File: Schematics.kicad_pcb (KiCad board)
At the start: 2 copper layers, 56 parts, among them Q1 AO3400A, Q2 SI2301CDS-T1-E3, Q3 SI2301CDS-T1-E3, Q4 8050

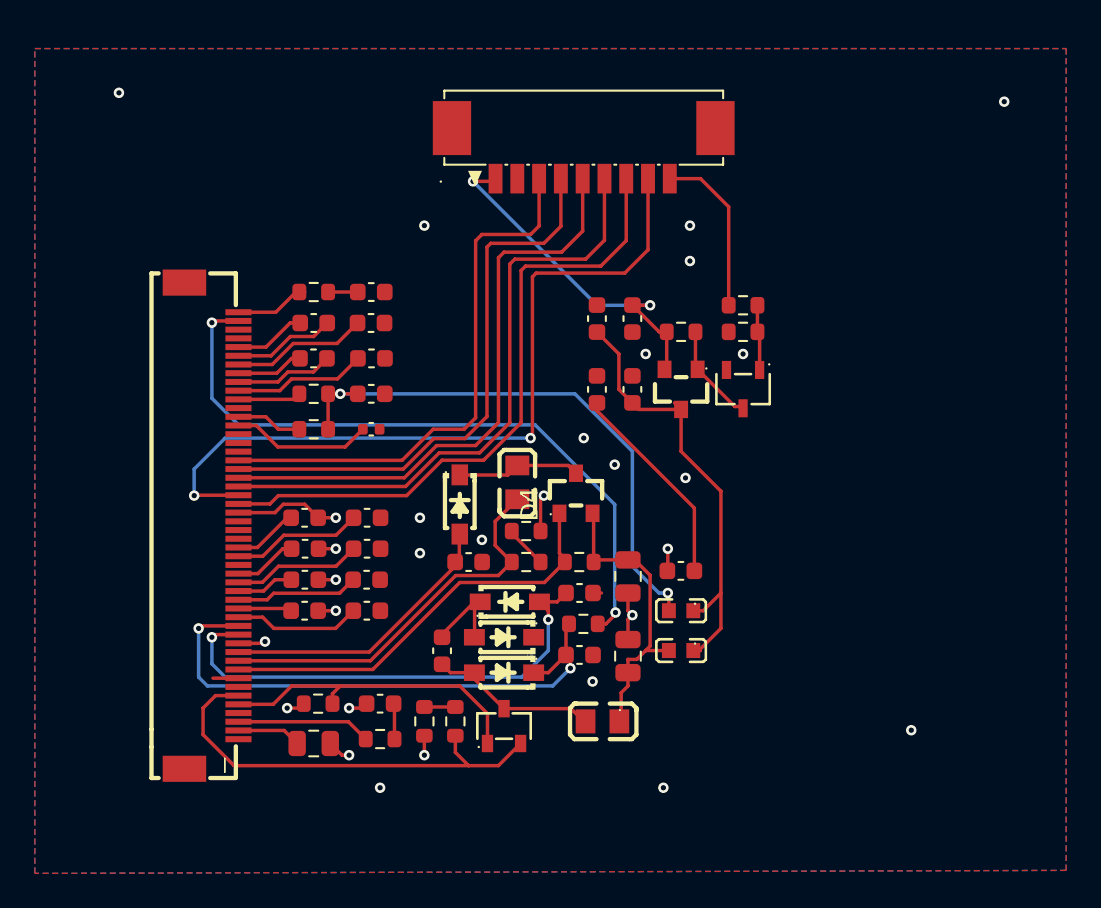
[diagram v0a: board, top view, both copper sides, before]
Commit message: added edge cuts and connected 2 unconnected ground pins
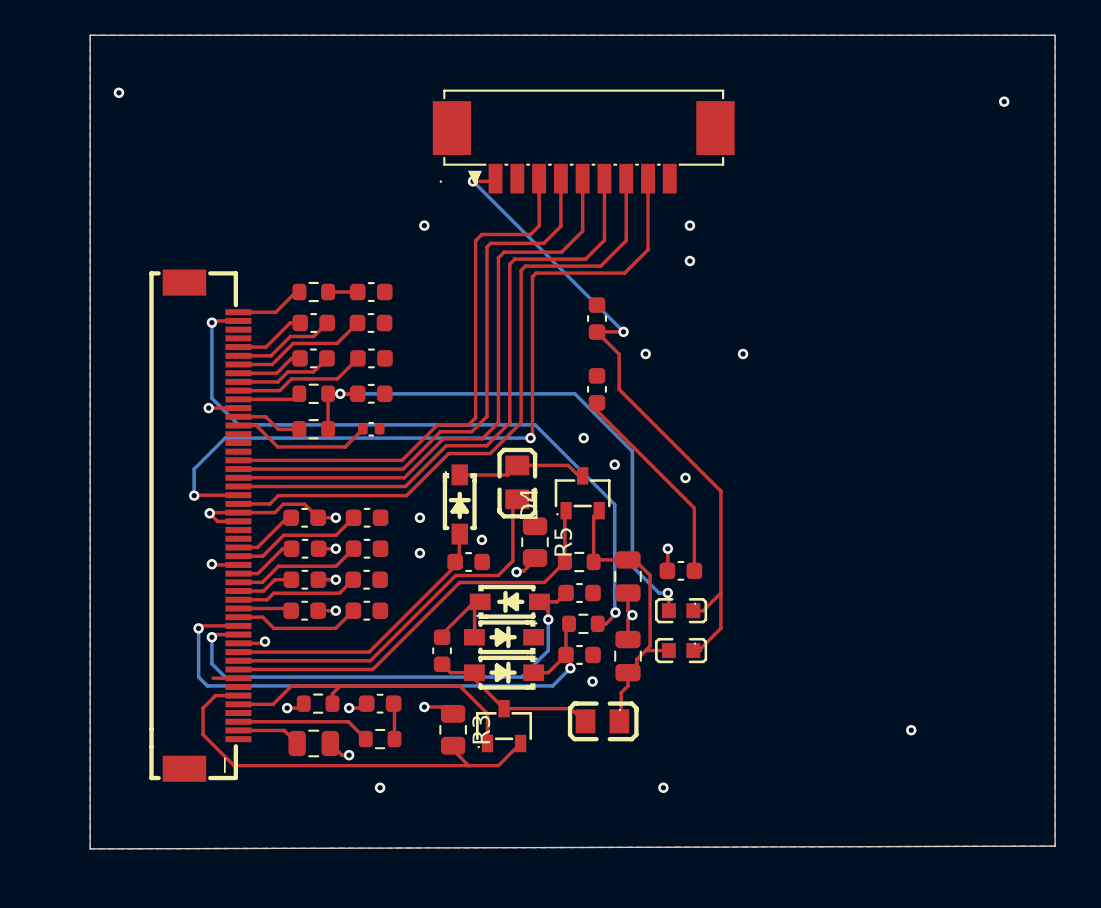
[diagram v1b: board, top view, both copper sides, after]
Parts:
- removed C22, C26: 100nF/50V, Capacitor_SMD:C_0603_1608Metric
- removed Q3: SI2301CDS-T1-E3, local:SOT-23_L2.9-W1.3-P1.90-LS2.4-BR
- removed Q4: 8050, local:SOT-23-3_L3.0-W1.7-P0.95-LS2.9-BR
- removed R11: 100K, Resistor_SMD:R_0603_1608Metric
- removed R6: 47K, Resistor_SMD:R_0603_1608Metric
- removed R7, R9: 0.1Ω, Resistor_SMD:R_0603_1608Metric
- removed R8: 10K, Resistor_SMD:R_0603_1608Metric
- Q2: value SI2301CDS-T1-E3 -> AO3401A; footprint local:SOT-23_L2.9-W1.3-P1.90-LS2.4-BR -> local:SOT-23-3_L2.9-W1.3-P1.90-LS2.4-BR
- R3, R5: value 0.1Ω -> 0.22Ω; footprint Resistor_SMD:R_0603_1608Metric -> Resistor_SMD:R_0805_2012Metric
- moved R5 0.81 mm to (77.5, 61.8), turned to -90 degrees
- moved R3 0.50 mm to (72.8, 72.6)
- moved Q2 0.38 mm to (80.2, 59.0)
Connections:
- P2 pad 1: /VCC_INT -> VCC
- R3 pad 1: Net-(R3-Pad1) -> GND
- R5 pad 1: Net-(R5-Pad1) -> /RESEC
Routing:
- net /VCC_INT: track 20.3 -> 0.00 mm, vias 2 -> 0
- net VCC: track 26.2 -> 39.3 mm, vias 0 -> 2
- net /PWR: track 10.1 -> 0.00 mm
- net GND: track 23.1 -> 29.4 mm, vias 29 -> 32
- net Net-(Q3-G): track 5.52 -> 0.00 mm
- net Net-(Q4-B): track 3.86 -> 0.00 mm
- net /RESEC: track 22.6 -> 25.2 mm
- net Net-(R5-Pad1): track 2.46 -> 0.00 mm
- net Net-(R3-Pad1): track 1.78 -> 0.00 mm
- net /RESEH: track 25.4 -> 24.8 mm
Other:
- board outline added: 55.4 x 46.7 mm

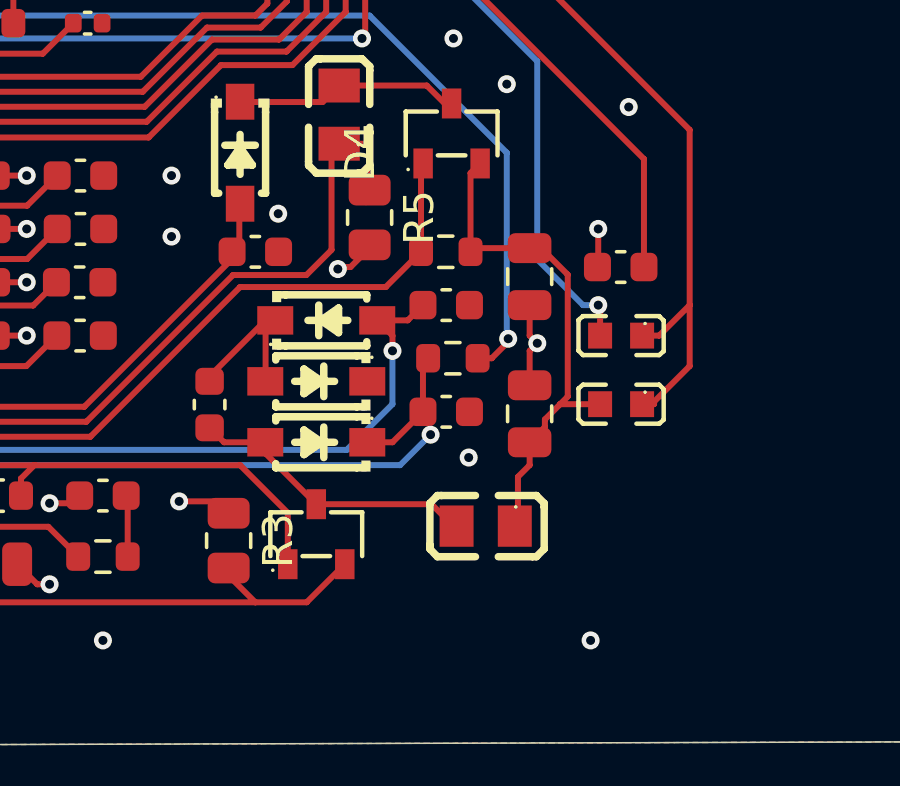
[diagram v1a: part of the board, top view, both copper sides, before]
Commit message: added missing capacitor
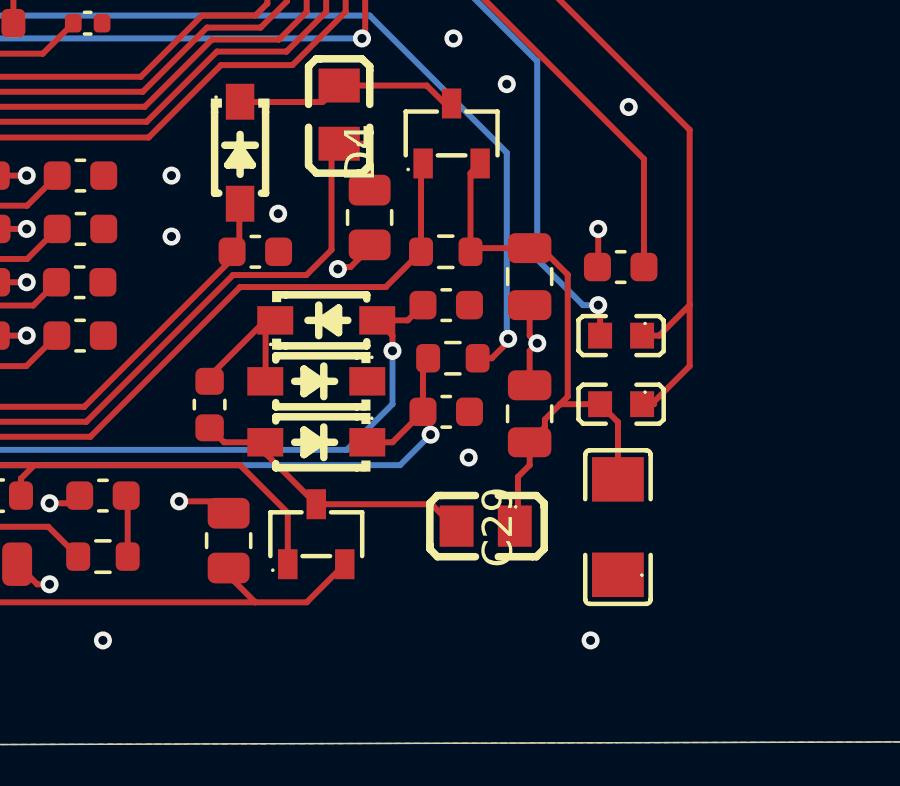
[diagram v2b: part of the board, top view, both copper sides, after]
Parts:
- added C29: 100uF/6.3V, local:C1206, F.Cu at (85.7, 72.2)
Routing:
- net V_B: track 17.2 -> 19.9 mm
